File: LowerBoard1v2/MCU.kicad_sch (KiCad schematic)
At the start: 109 parts, among them J401 PWR, J402 DATA, J403 SWD Header, J404 MIDI_In, J405 Micro_SD_Card_Det2, J406 MIDI_Out, J407 MIDI_Thru, J408 POWER, Q401 2N7002H, Q402 2N7002H, SW401 RST, SW402 BOOT, U401 STM32F411RET6, U402 TPS56528DDA, U403 AMS1117, U404 74HC04, U405 6N138, Y401 16MHz, Y402 32.768kHZ

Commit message: power supply and load switch stuff
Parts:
- removed C427: 100n, Capacitor_SMD:C_0805_2012Metric, symbol Device:C
- removed J401: PWR, Connector_PinHeader_2.54mm:PinHeader_1x05_P2.54mm_Vertical, symbol Connector:Conn_01x05_Pin
- removed J402: DATA, Connector_PinHeader_2.54mm:PinHeader_1x03_P2.54mm_Vertical, symbol Connector:Conn_01x03_Pin
- removed U403: AMS1117, Package_TO_SOT_SMD:SOT-223-3_TabPin2, symbol Regulator_Linear:AMS1117
- added D407: MMSZ5227C, Diode_SMD:D_SOD-123, symbol Device:D_Zener
- added D408: PMEG3030, Diode_SMD:D_SOD-123, symbol Device:D_Schottky
- added FB402: 21R, Inductor_SMD:L_0805_2012Metric, symbol Device:FerriteBead
- added J401: Conn_01x02_Pin, Connector_PinHeader_2.54mm:PinHeader_1x02_P2.54mm_Vertical, symbol Connector:Conn_01x02_Pin
- added Q403: BSH205G2A, PCM_4ms_Package_SOT:SOT-23, symbol Device:Q_PMOS_GSD
- added R403, R404, R406: 10k, Resistor_SMD:R_0805_2012Metric, symbol Device:R_US
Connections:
- net +3.3V: now also D407.1 (K), FB402.1; no longer D404.1 (K)
- net BATT_REF: now also J401.1 (Pin_1)
- net GND: now also C426.2, D407.2 (A), J401.2 (Pin_2), R403.2, R404.2, R406.2; no longer C426.1
- net LED1: now also R404.1
- net LED2: now also R406.1
- net at C422.1, C423.1, L401.2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: now also FB402.2; no longer D404.2 (A)
- net V_SWD: now reaches J403.1 (Pin_1)
- net V_SWD: now also D404.2 (A), Q403.1 (G), R403.1; no longer C426.2
- net +12VA renamed VDD
- net VDD: now also C426.1, D404.1 (K), D408.1 (K); no longer D403.2 (A), J408.1 (Pin_1), J408.2 (Pin_2)
- net USB_D+: no longer names the net of U401.45 (PA12)
- net USB_D-: no longer names the net of U401.44 (PA11)
- new net: D408.2 (A), Q403.3 (D)
- new net V_EURO: D403.2 (A), J408.1 (Pin_1), J408.2 (Pin_2), Q403.2 (S)
- no-connect marks 18 -> 20
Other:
- note added: "Power Input (Eurorack 10 pin)"
- note removed: "Power Input A (Standalone)"
- note removed: "Power Input B (Eurorack)"
- moved on the sheet: C404, C418, C419, C420, C421, C422, C423, D402, D403, D405, D406, J403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

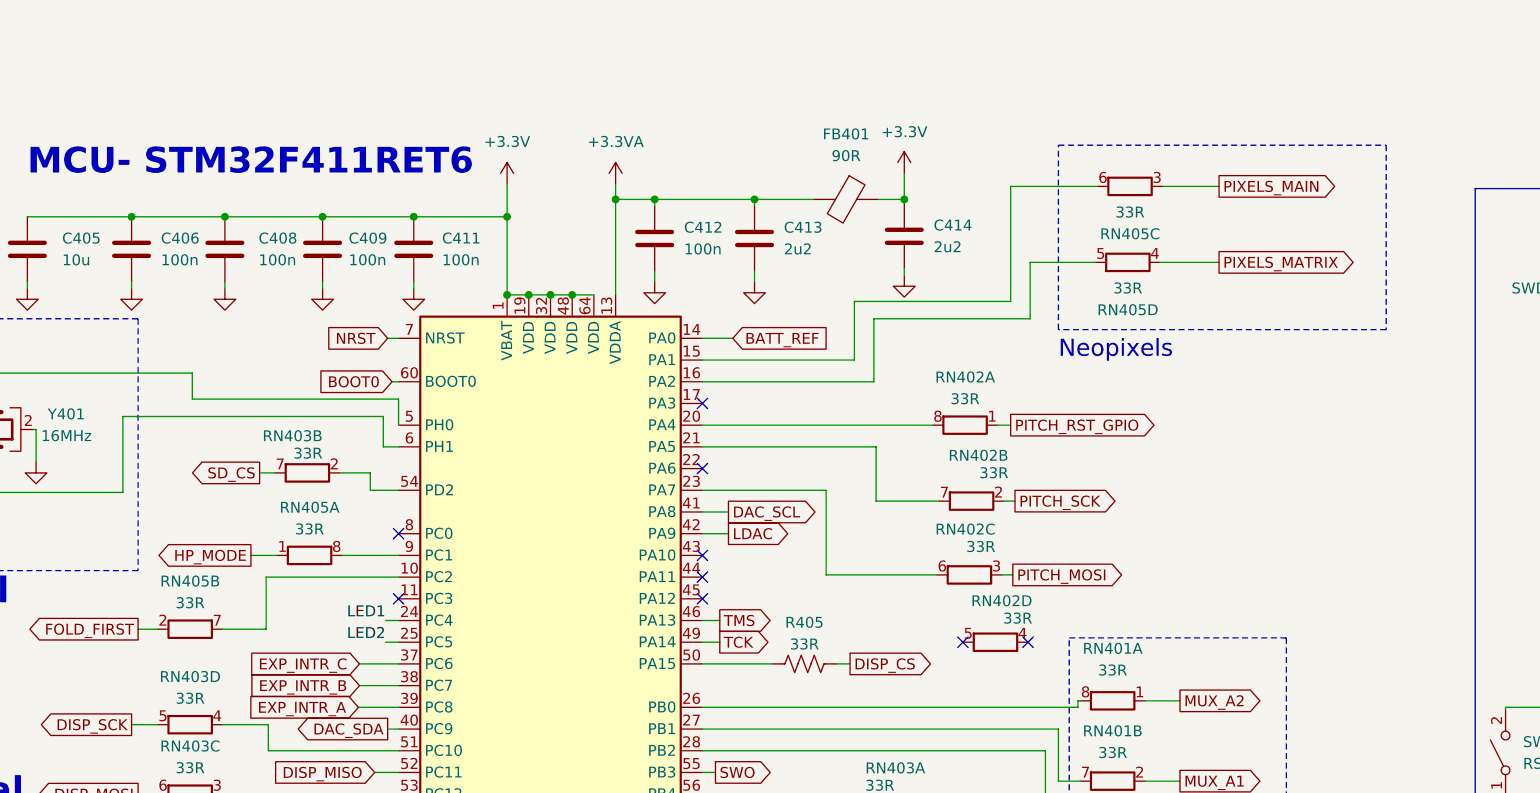
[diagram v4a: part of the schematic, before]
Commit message: central mux routing
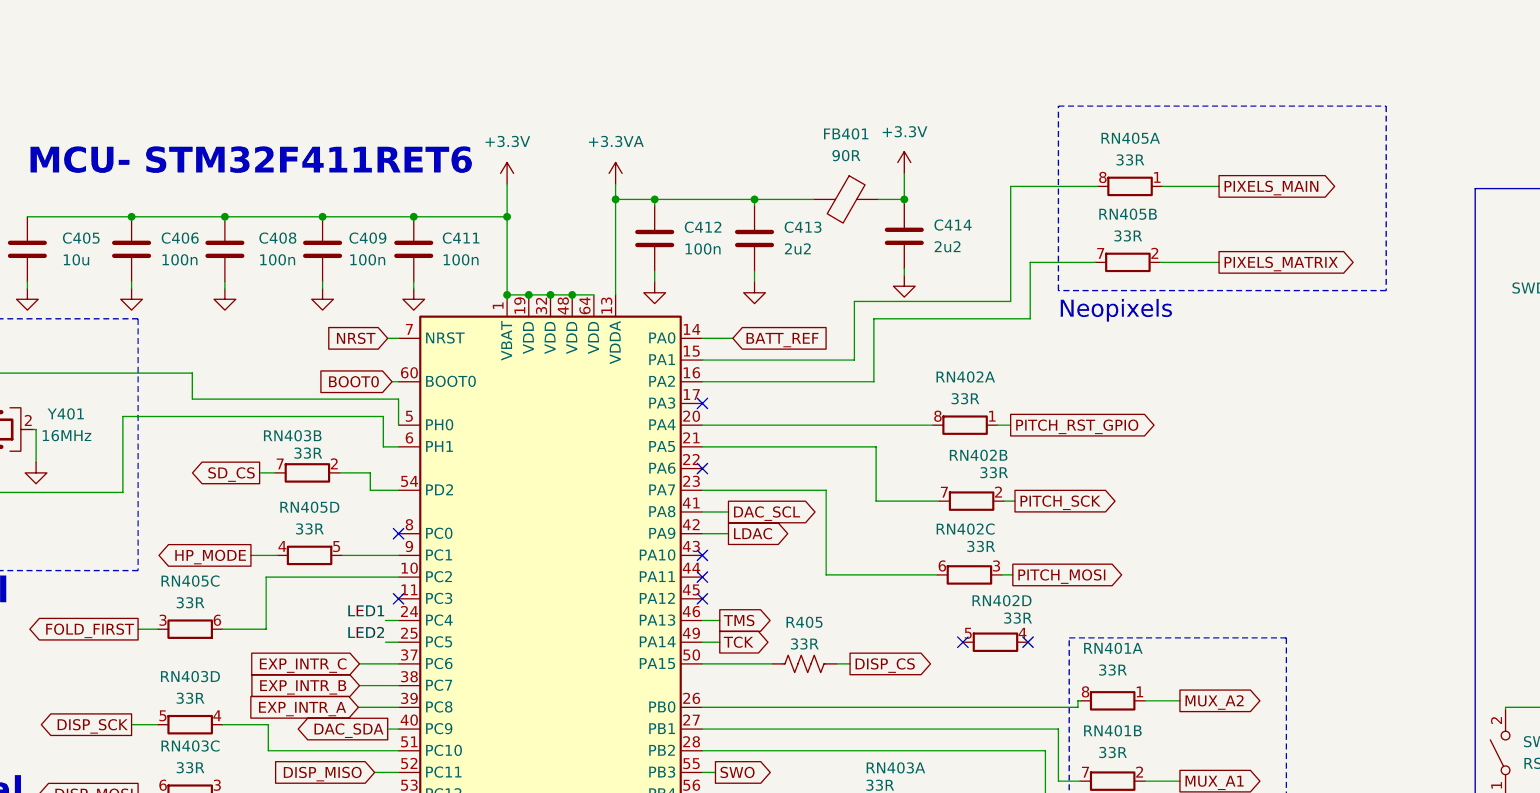
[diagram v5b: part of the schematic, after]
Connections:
- net FOLD_FIRST: now also RN405.3 (R3.1); no longer RN405.2 (R2.1)
- net HP_MODE: now also RN405.4 (R4.1); no longer RN405.1 (R1.1)
- net PIXELS_MAIN: now also RN405.1 (R1.1); no longer RN405.3 (R3.1)
- net PIXELS_MATRIX: now also RN405.2 (R2.1); no longer RN405.4 (R4.1)
- net at U401.10 (PC2): now also RN405.6 (R3.2); no longer RN405.7 (R2.2)
- net at U401.15 (PA1): now also RN405.8 (R1.2); no longer RN405.6 (R3.2)
- net at U401.16 (PA2): now also RN405.7 (R2.2); no longer RN405.5 (R4.2)
- net at U401.9 (PC1): now also RN405.5 (R4.2); no longer RN405.8 (R1.2)
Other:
- moved on the sheet: RN405A, RN405B, RN405C, RN405D
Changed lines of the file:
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@@
 	)
 	(rectangle
-		(start 169.418 29.972)
-		(end 207.772 51.562)
+		(start 169.418 25.4)
+		(end 207.772 46.99)
 		(stroke
 			(width 0)
@@
 	(text "Neopixels"
 		(exclude_from_sim no)
-		(at 169.418 55.118 0)
+		(at 169.418 50.546 0)
 		(effects
 			(font
@@
 	(symbol
 		(lib_id "Device:R_Pack04_Split")
-		(at 81.788 77.978 270)
-		(mirror x)
+		(at 177.8 34.798 90)
 		(unit 1)
 		(exclude_from_sim no)
@@
 		(dnp no)
 		(property "Reference" "RN405"
-			(at 81.788 72.39 90)
+			(at 177.8 29.21 90)
 			(effects
 				(font
@@
 		)
 		(property "Value" "33R"
-			(at 81.788 74.93 90)
+			(at 177.8 31.75 90)
 			(effects
 				(font
@@
 		)
 		(property "Footprint" "Resistor_SMD:R_Array_Concave_4x0603"
-			(at 81.788 80.01 90)
+			(at 177.8 36.83 90)
 			(effects
 				(font
@@
 		)
 		(property "Datasheet" "~"
-			(at 81.788 77.978 0)
+			(at 177.8 34.798 0)
 			(effects
 				(font
@@
 		)
 		(property "Description" "4 resistor network, parallel topology, split"
-			(at 81.788 77.978 0)
+			(at 177.8 34.798 0)
 			(effects
 				(font
@@
 	(symbol
 		(lib_id "Device:R_Pack04_Split")
-		(at 67.818 86.614 270)
-		(mirror x)
+		(at 177.546 43.688 90)
 		(unit 2)
 		(exclude_from_sim no)
@@
 		(dnp no)
 		(property "Reference" "RN405"
-			(at 67.818 81.026 90)
+			(at 177.546 38.1 90)
 			(effects
 				(font
@@
 		)
 		(property "Value" "33R"
-			(at 67.818 83.566 90)
+			(at 177.546 40.64 90)
 			(effects
 				(font
@@
 		)
 		(property "Footprint" "Resistor_SMD:R_Array_Concave_4x0603"
-			(at 67.818 88.646 90)
+			(at 177.546 45.72 90)
 			(effects
 				(font
@@
 		)
 		(property "Datasheet" "~"
-			(at 67.818 86.614 0)
+			(at 177.546 43.688 0)
 			(effects
 				(font
@@
 		)
 		(property "Description" "4 resistor network, parallel topology, split"
-			(at 67.818 86.614 0)
+			(at 177.546 43.688 0)
 			(effects
 				(font
@@
 	(symbol
 		(lib_id "Device:R_Pack04_Split")
-		(at 177.8 34.798 90)
+		(at 67.818 86.614 270)
 		(unit 3)
 		(exclude_from_sim no)
@@
 		(dnp no)
 		(property "Reference" "RN405"
-			(at 177.8 40.386 90)
+			(at 67.818 81.026 90)
 			(effects
 				(font
@@
 		)
 		(property "Value" "33R"
-			(at 177.8 37.846 90)
+			(at 67.818 83.566 90)
 			(effects
 				(font
@@
 		)
 		(property "Footprint" "Resistor_SMD:R_Array_Concave_4x0603"
-			(at 177.8 36.83 90)
+			(at 67.818 84.582 90)
 			(effects
 				(font
@@
 		)
 		(property "Datasheet" "~"
-			(at 177.8 34.798 0)
+			(at 67.818 86.614 0)
 			(effects
 				(font
@@
 		)
 		(property "Description" "4 resistor network, parallel topology, split"
-			(at 177.8 34.798 0)
+			(at 67.818 86.614 0)
 			(effects
 				(font
@@
 	(symbol
 		(lib_id "Device:R_Pack04_Split")
-		(at 177.546 43.688 90)
+		(at 81.788 77.978 270)
 		(mirror x)
 		(unit 4)
@@
 		(dnp no)
 		(property "Reference" "RN405"
-			(at 177.546 49.276 90)
+			(at 81.788 72.39 90)
 			(effects
 				(font
@@
 		)
 		(property "Value" "33R"
-			(at 177.546 46.736 90)
+			(at 81.788 74.93 90)
 			(effects
 				(font
@@
 		)
 		(property "Footprint" "Resistor_SMD:R_Array_Concave_4x0603"
-			(at 177.546 41.656 90)
+			(at 81.788 80.01 90)
 			(effects
 				(font
@@
 		)
 		(property "Datasheet" "~"
-			(at 177.546 43.688 0)
+			(at 81.788 77.978 0)
 			(effects
 				(font
@@
 		)
 		(property "Description" "4 resistor network, parallel topology, split"
-			(at 177.546 43.688 0)
+			(at 81.788 77.978 0)
 			(effects
 				(font
